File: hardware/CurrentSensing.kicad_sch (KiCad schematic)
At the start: 0 parts

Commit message: Populate Current Sensing + Communication sheets; schematic complete
Current Sensing:
- DC-bus shunt (5 mOhm, in series after the eFuse - required renaming
  the eFuse OUT net to +VBUS_EFUSE_OUT so the shunt sits properly
  in-line ahead of +VBUS_PROT)
- INA240 total-bus current sense, unidirectional config, -> MCU ADC

Communication:
- SN65HVD230 CAN transceiver (3.3V native) on ESP32 TWAI pins
- Per-line TVS (SP0115-01UTG) on CANH/CANL
- 4-pin bus connector (CANH/CANL/GND/+VBUS_PROT)

Whole-hierarchy ERC (all 6 sheets + root) now down to 3 residual
errors, all the same benign/expected 'two power_out pins on one net'
pattern (datasheet-recommended parallel pins, or a PWR_FLAG sharing
a net with a real driver) - fully explained in ARCHITECTURE.md, which
now also documents the found-and-worked-around vendor library defects
(eFuse pin-20 duplication, TMP235 VOUT mistyped as input) and confirms
the shunt 'duplicate pins' are correct 4-terminal Kelvin modeling, not
a bug.

All 6 hierarchical sheets are now fully wired end to end:
Power Supply -> MCU Core -> Gate Drive -> Power Stage, with Current
Sensing and Communication cross-wired throughout.

Co-Authored-By: Claude Sonnet 5 <noreply@anthropic.com>
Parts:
- added C33: INA240 decouple, symbol METUPowerLab_Capacitors_Ceramics_SurfaceMounts:100 nF
- added RS4: DC bus shunt, METUPowerLab_Resistors_ShuntResistors:2010, symbol METUPowerLab_Resistors_ShuntResistors:5 mOhm
- added U9: INA240A4DR, METUPowerLab_Amplifiers_CurrentSenses:8-SOIC, symbol METUPowerLab_Amplifiers_CurrentSenses:INA240A4DR
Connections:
- new net +3V3_MCU: C33.1, U9.6 (V+)
- new net +VBUS_EFUSE_OUT: RS4.1, U9.8 (+)
- new net +VBUS_PROT: RS4.2, U9.1 (-)
- new net GND: C33.2, U9.2 (GND), U9.3 (REF2), U9.4 (GND), U9.7 (REF1)
- new net IBUS_SENSE: U9.5

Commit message: PCB layout: board outline, mounting holes, footprint placement, copper pours, phase-output routing
- 100x115mm 2-layer board, 4x M3 mounting holes, design rules per PowerLab spec
- All 55 schematic components synced to board with real footprints
- Auto-placed via force-directed placement with locked connector/MCU anchors
- GND pour (both layers) + localized pours for VIN_RAW/+VBUS/+VBUS_EFUSE_OUT/+VBUS_PROT/+5V_LOGIC
- Routed the 3 critical phase-output traces (SHA/SHB/SHC, 2mm wide)
- Documented full PCB status in ARCHITECTURE.md: NOT yet fab-ready (732 DRC
  violations, 21 courtyard overlaps, ~50 signal nets still unrouted since
  Freerouting is unavailable in this environment)

Co-Authored-By: Claude Sonnet 5 <noreply@anthropic.com>
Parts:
- C33: footprint (none) -> METUPowerLab_Capacitors_Ceramics_SurfaceMounts:0603_Medium
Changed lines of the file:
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@@
 			)
 		)
-		(property "Footprint" ""
+		(property "Footprint" "METUPowerLab_Capacitors_Ceramics_SurfaceMounts:0603_Medium"
 			(at 101.295 38.1 0)
 			(hide yes)

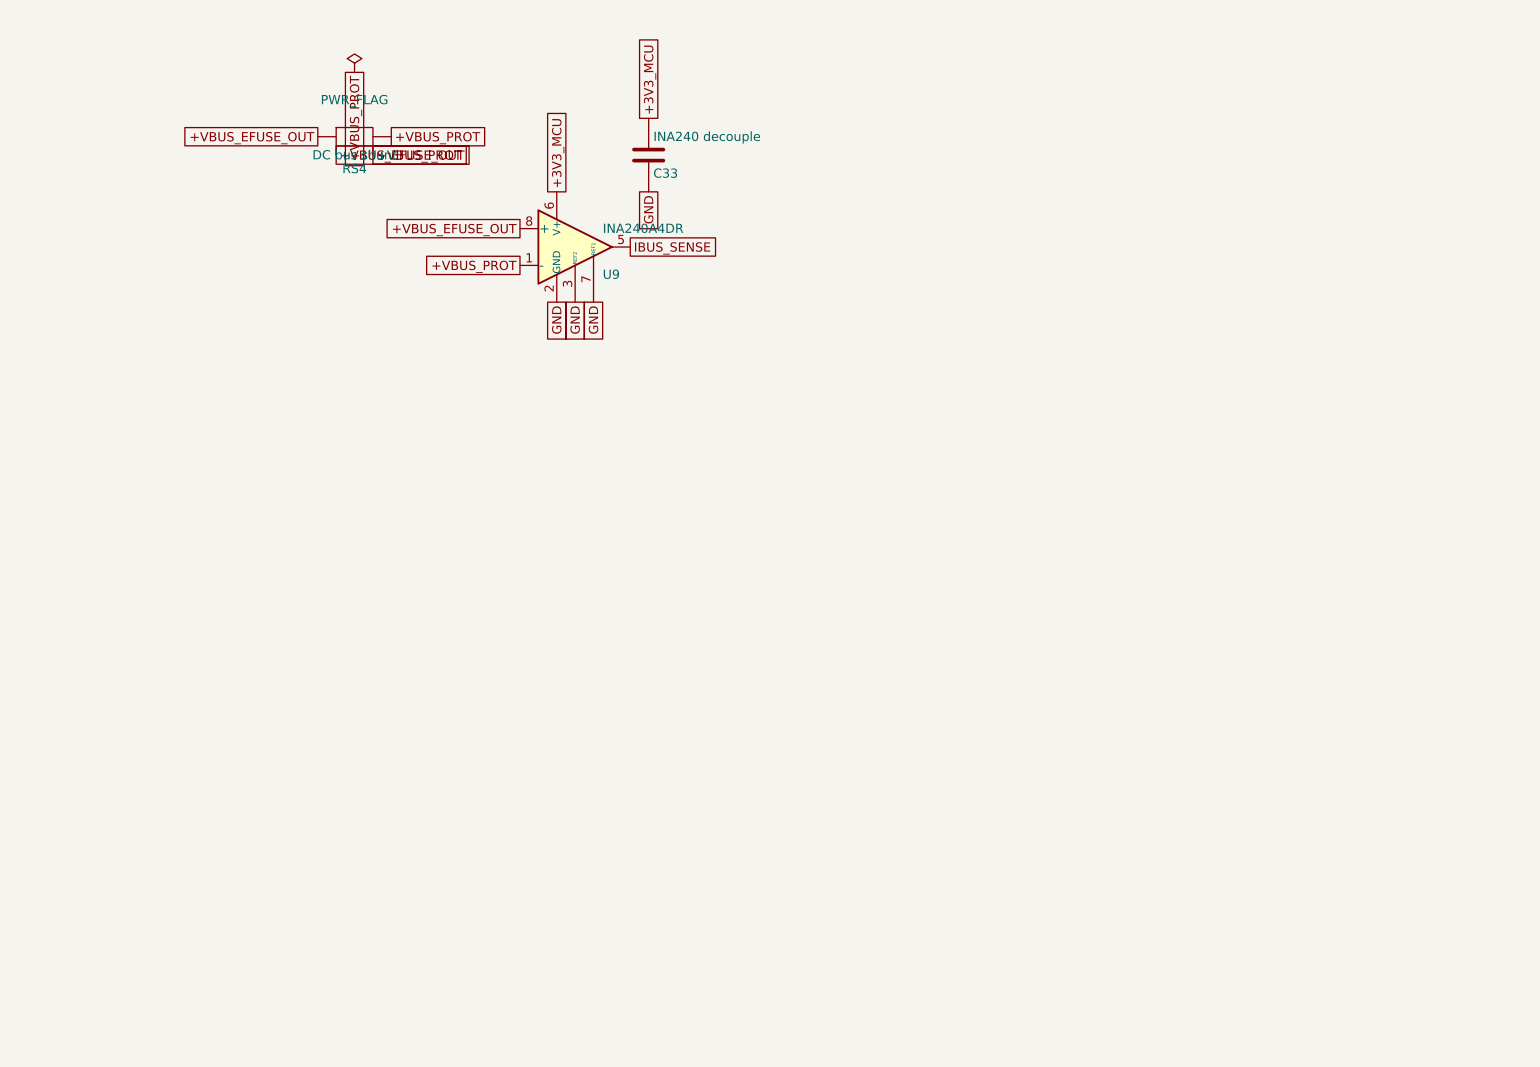
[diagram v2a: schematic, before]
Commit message: Schematic Rev B: full rebuild per METU PowerLab rules
Rev A was withdrawn: labels stuck on pins created real net shorts
(+5V_LOGIC with the 36 V bus, INHA and EFUSE_IMON with GND) and several
circuits contradicted their datasheets.

Rev B: real wires and power symbols on the 2.54 mm grid, hierarchical sheets
(half bridge reused 3x), library values, LAYOUT notes, root page with specs
and block diagram. Circuit fixes: DRV8323 VREF driven, unused buck tied to
GND, INA240A1, LM74700-Q1 reverse polarity, SMBJ36CA, eFuse per datasheet,
direct 3.3 V buck, 4.7 uH/8.1 A inductor, 2512 shunts with net-tie Kelvin,
24 V CAN ESD. kicad-cli ERC: 0 errors; netlist matches intent on all nets.
Old board and project-local library tables removed (board is rebuilt next).

Co-Authored-By: Claude Opus 5.5 <noreply@anthropic.com>
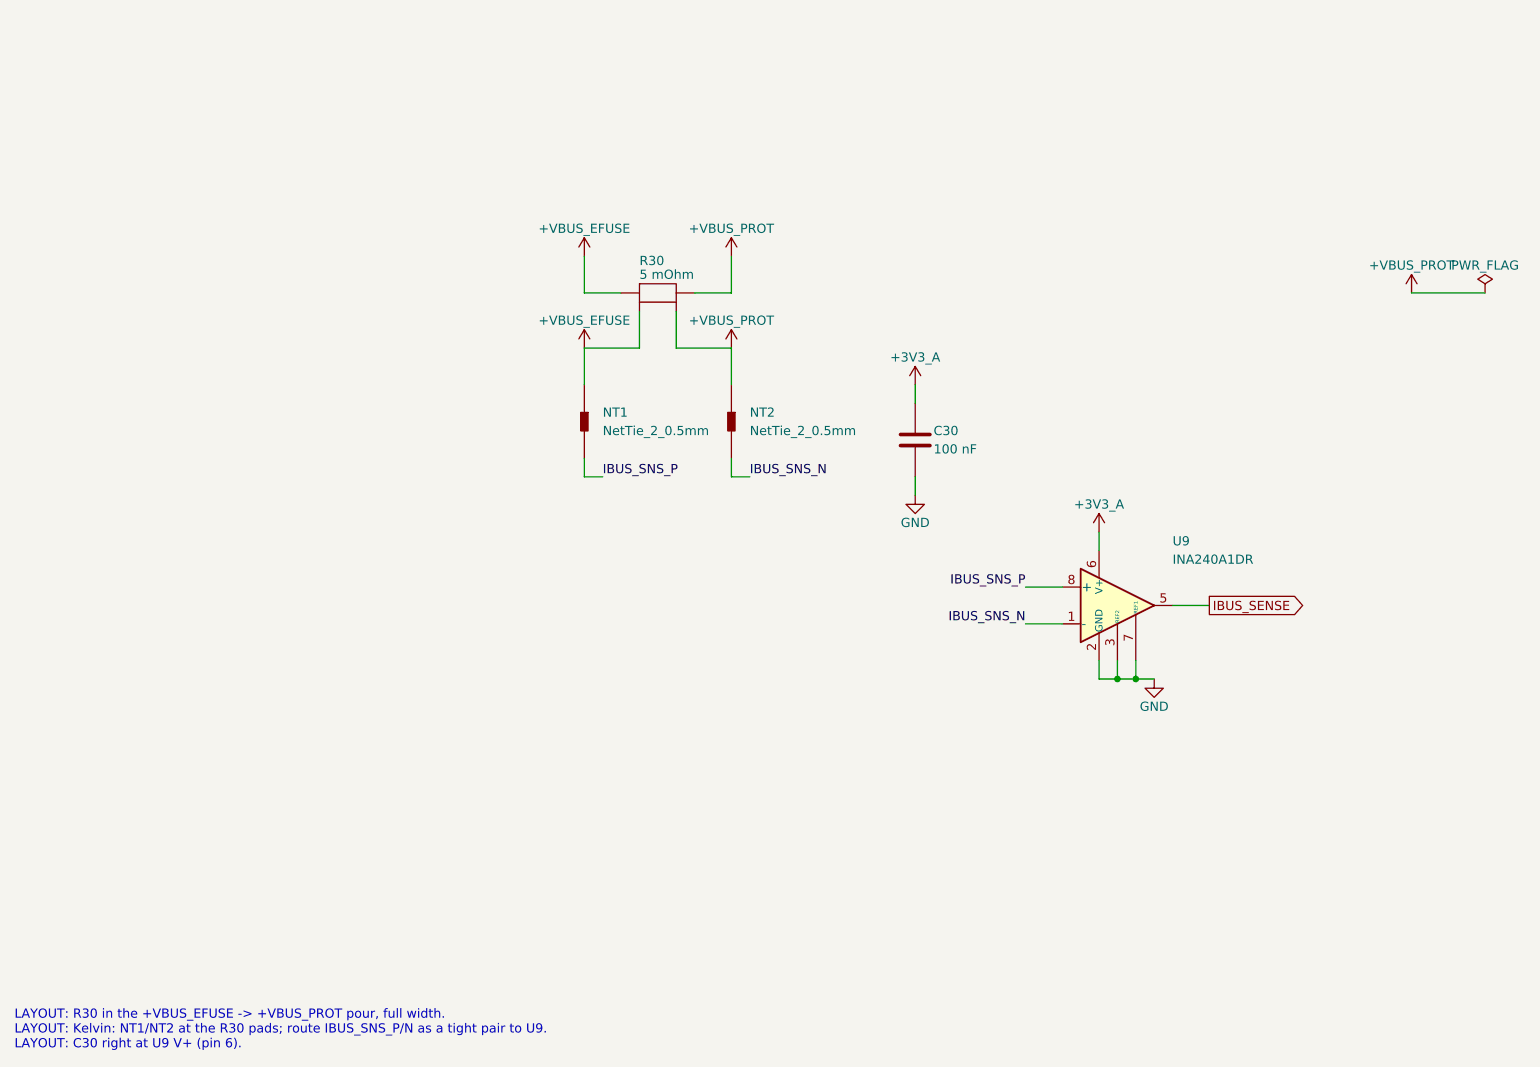
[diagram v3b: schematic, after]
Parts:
- removed C33: INA240 decouple, METUPowerLab_Capacitors_Ceramics_SurfaceMounts:0603_Medium, symbol METUPowerLab_Capacitors_Ceramics_SurfaceMounts:100 nF
- removed RS4: DC bus shunt, METUPowerLab_Resistors_ShuntResistors:2010, symbol METUPowerLab_Resistors_ShuntResistors:5 mOhm
- removed U9: INA240A4DR, METUPowerLab_Amplifiers_CurrentSenses:8-SOIC, symbol METUPowerLab_Amplifiers_CurrentSenses:INA240A4DR
- added C30: 100 nF, METUPowerLab_Capacitors_Ceramics_SurfaceMounts:0603_Medium, symbol METUPowerLab_Capacitors_Ceramics_SurfaceMounts:100 nF
- added NT1, NT2: NetTie_2_0.5mm, METUPowerLab_NetTies_SurfaceMounts:NetTie_2_0.5mm, symbol METUPowerLab_NetTies_SurfaceMounts:NetTie_2_0.5mm
- added R30: 5 mOhm, METUPowerLab_Resistors_ShuntResistors:2010, symbol METUPowerLab_Resistors_ShuntResistors:5 mOhm
- added U9: INA240A1DR, METUPowerLab_Amplifiers_CurrentSenses:8-SOIC, symbol METUPowerLab_Amplifiers_CurrentSenses:INA240A1DR
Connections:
- net +VBUS_PROT: now also NT2.1, R30.2
- net GND: now also C30.2, U9.2 (GND), U9.3 (REF2), U9.4 (GND), U9.7 (REF1)
- net IBUS_SENSE: now also U9.5
- new net +3V3_A: C30.1, U9.6 (V+)
- new net +VBUS_EFUSE: NT1.1, R30.1
- new net IBUS_SNS_N: NT2.2, U9.1 (-)
- new net IBUS_SNS_P: NT1.2, U9.8 (+)
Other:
- note added: "LAYOUT: R30 in the +VBUS_EFUSE -> +VBUS_PROT pour, full width. LAYOUT: Kelvin: NT1/NT2 at the R30 pads; route IBUS_SNS_P/N as a tight pair to U9. LAYOUT: C30 right at U9 V+ (pin 6)."
- title: ${PROJECT_NAME} -> DC-Bus Current Sensing
